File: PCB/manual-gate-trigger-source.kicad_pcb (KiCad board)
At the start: 2 copper layers, 182.9 x 110.5 mm, 135 parts, among them J1 PWR, J10 IN1, J11 Conn_01x04, J12 Conn_01x04, J13 PWR_BRD, J14 INT_BRD, J2 OUTa, J3 OUTb, J4 OUTa, J5 OUTb, J6 OUTa, J7 OUTb, J8 OUTa, J9 OUTb, Q1 BC547, Q2 BC547, Q3 BC547, Q4 BC547, Q5 BC547, Q6 BC547, SW1 ON/OFF/ON, SW2 ON/ON, SW3 ON/ON, SW4 ON/ON, SW5 ON/ON, SW6 SW_Push, SW7 SW_Push, SW8 SW_Push, U1 TL072, U2 LM555xN, U3 LM555xN, U4 LM555xN, U5 LM555xN

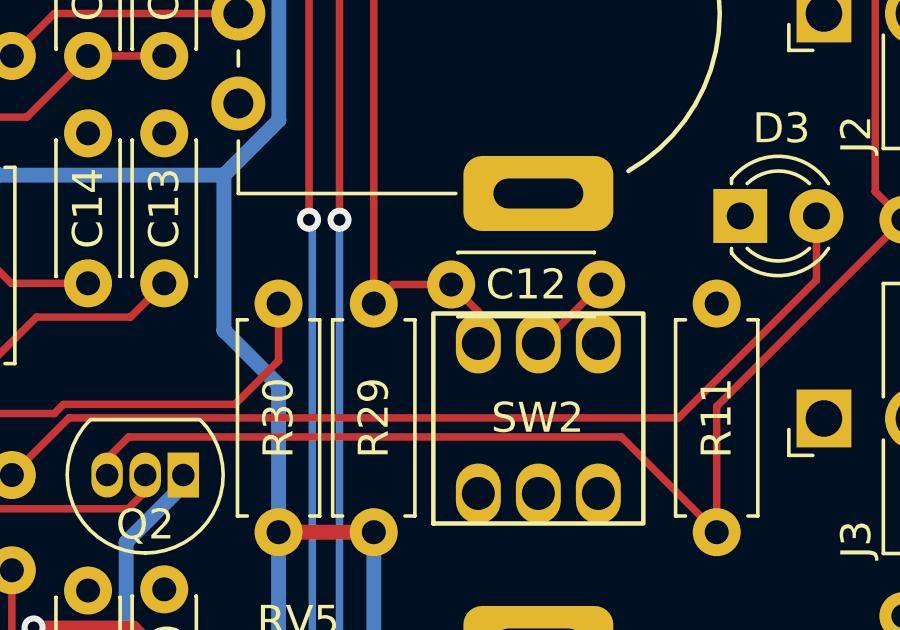
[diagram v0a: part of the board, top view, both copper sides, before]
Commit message: :bug: Fix a missing connection
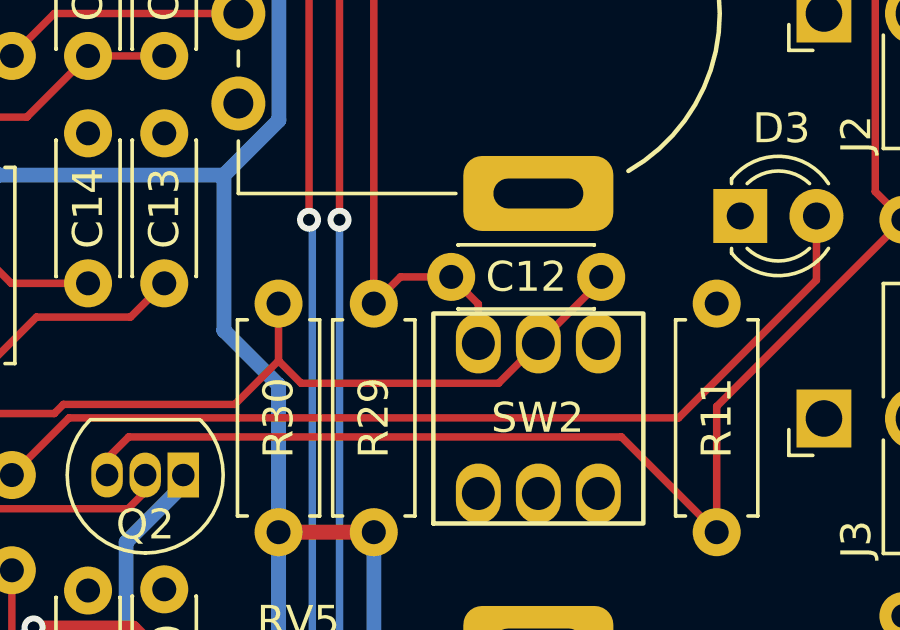
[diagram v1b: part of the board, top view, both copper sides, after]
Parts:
- moved C12 0.25 mm to (132.2, 57.8)
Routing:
- net Net-(SW2-A): track 25.9 -> 35.6 mm
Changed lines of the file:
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@@
   )
   (footprint "Capacitor_THT:C_Disc_D4.3mm_W1.9mm_P5.00mm" (layer "F.Cu")
-    (at 132.195 58.035)
+    (at 132.195 57.781)
     (descr "C, Disc series, Radial, pin pitch=5.00mm, , diameter*width=4.3*1.9mm^2, Capacitor, http://www.vishay.com/docs/45233/krseries.pdf")
     (tags "C Disc series Radial pin pitch 5.00mm  diameter 4.3mm width 1.9mm Capacitor")
@@
   (segment (start 126.402792 43.39) (end 109.97 43.39) (width 0.25) (layer "F.Cu") (net 5))
   (segment (start 129.615 58.67) (end 129.615 46.602208) (width 0.25) (layer "F.Cu") (net 5))
+  (segment (start 130.504 57.781) (end 129.615 58.67) (width 0.25) (layer "F.Cu") (net 5))
+  (segment (start 132.195 57.781) (end 130.504 57.781) (width 0.25) (layer "F.Cu") (net 5))
   (segment (start 129.615 46.602208) (end 126.402792 43.39) (width 0.25) (layer "F.Cu") (net 5))
+  (segment (start 133.1 58.686) (end 132.195 57.781) (width 0.25) (layer "F.Cu") (net 5))
   (segment (start 109.97 43.39) (end 106.755 46.605) (width 0.25) (layer "F.Cu") (net 5))
-  (segment (start 133.1 58.94) (end 132.195 58.035) (width 0.25) (layer "F.Cu") (net 5))
-  (segment (start 133.1 60) (end 133.1 58.94) (width 0.25) (layer "F.Cu") (net 5))
-  (segment (start 130.25 58.035) (end 129.615 58.67) (width 0.25) (layer "F.Cu") (net 5))
-  (segment (start 132.195 58.035) (end 130.25 58.035) (width 0.25) (layer "F.Cu") (net 5))
+  (segment (start 133.1 60) (end 133.1 58.686) (width 0.25) (layer "F.Cu") (net 5))
+  (segment (start 127.19 61.325) (end 126.44 60.575) (width 0.25) (layer "F.Cu") (net 6))
   (segment (start 124.985 62.03) (end 126.44 60.575) (width 0.25) (layer "F.Cu") (net 6))
   (segment (start 109.16 60.075) (end 111.335 60.075) (width 0.25) (layer "F.Cu") (net 6))
+  (segment (start 137.195 57.781) (end 137.195 57.905) (width 0.25) (layer "F.Cu") (net 6))
   (segment (start 119.268604 62.03) (end 124.985 62.03) (width 0.25) (layer "F.Cu") (net 6))
+  (segment (start 137.195 57.905) (end 135.1 60) (width 0.25) (layer "F.Cu") (net 6))
   (segment (start 108.035 61.2) (end 109.16 60.075) (width 0.25) (layer "F.Cu") (net 6))
   (segment (start 111.335 60.075) (end 111.99 60.73) (width 0.25) (layer "F.Cu") (net 6))
-  (segment (start 137.195 58.035) (end 135.23 60) (width 0.25) (layer "F.Cu") (net 6))
+  (segment (start 135.1 60) (end 133.775 61.325) (width 0.25) (layer "F.Cu") (net 6))
   (segment (start 111.99 61.665991) (end 112.659009 62.335) (width 0.25) (layer "F.Cu") (net 6))
-  (segment (start 135.23 60) (end 135.1 60) (width 0.25) (layer "F.Cu") (net 6))
   (segment (start 111.99 60.73) (end 111.99 61.665991) (width 0.25) (layer "F.Cu") (net 6))
   (segment (start 126.44 60.575) (end 126.44 58.67) (width 0.25) (layer "F.Cu") (net 6))
+  (segment (start 133.775 61.325) (end 127.19 61.325) (width 0.25) (layer "F.Cu") (net 6))
   (segment (start 112.659009 62.335) (end 118.963604 62.335) (width 0.25) (layer "F.Cu") (net 6))
   (segment (start 118.963604 62.335) (end 119.268604 62.03) (width 0.25) (layer "F.Cu") (net 6))

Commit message: :hammer: Adapt PCB to circuit changes
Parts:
- removed ? (x3): , 
- removed C11, C3: 100n, Capacitor_THT:C_Disc_D4.3mm_W1.9mm_P5.00mm
- removed C5: 10u, Capacitor_THT:CP_Radial_D4.0mm_P1.50mm
- removed D2: D_Schottky, Diode_THT:D_DO-41_SOD81_P7.62mm_Horizontal
- removed FB2: FerriteBead, moPsy:FBeadL4D4
- removed R6: 100R, Resistor_THT:R_Axial_DIN0207_L6.3mm_D2.5mm_P7.62mm_Horizontal
- removed R7: 10k, Resistor_THT:R_Axial_DIN0207_L6.3mm_D2.5mm_P7.62mm_Horizontal
- removed REF**: MountingHole_2.2mm_M2_DIN965_Pad, MountingHole:MountingHole_2.2mm_M2_DIN965_Pad
- R1: value 36k -> 71k5
- R2: value 75k -> 49k9
- R3: value 22k -> 39k
- R4: value 39k -> 44k2
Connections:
- U1 pad 1: Net-(R6-Pad2) -> Net-(Q1-B)
- U1 pad 2: Net-(U1A--) -> Vdrive
- U1 pad 4: -12V -> GND
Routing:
- net -12V: track 28.0 -> 0.00 mm
- net Net-(R6-Pad2): track 15.9 -> 0.00 mm
- net Net-(Q1-B): track 4.50 -> 16.6 mm
- net Net-(U1A--): track 8.46 -> 0.00 mm
- net Vdrive: track 114.1 -> 121.5 mm
- net /-12V_DIR: track 5.38 -> 0.00 mm
- net /-12V_IN: track 5.72 -> 2.54 mm
- net GND: vias 5 -> 14
